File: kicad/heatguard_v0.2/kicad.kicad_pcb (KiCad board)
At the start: 2 copper layers, 100 x 72 mm, 31 parts, among them J11 Conn_01x12, J12 Conn_01x12, J13 Conn_01x12, J14 Conn_01x12, J2 Conn_01x12, J20 Conn_01x01, J3 Conn_01x12, J4 Conn_01x12, J5 Conn_01x12, J6 Conn_01x12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

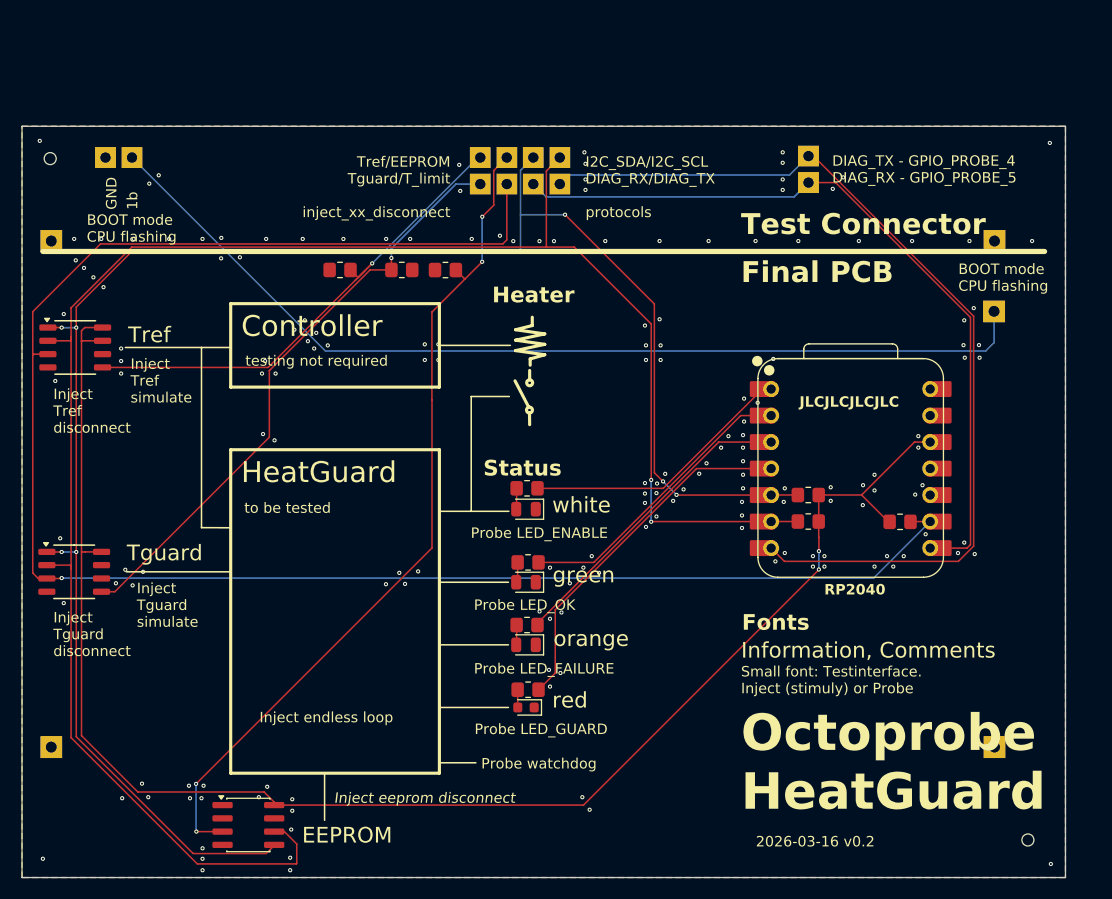
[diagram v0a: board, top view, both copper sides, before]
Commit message: v0.2: XIAO: Now smd (was on pins)
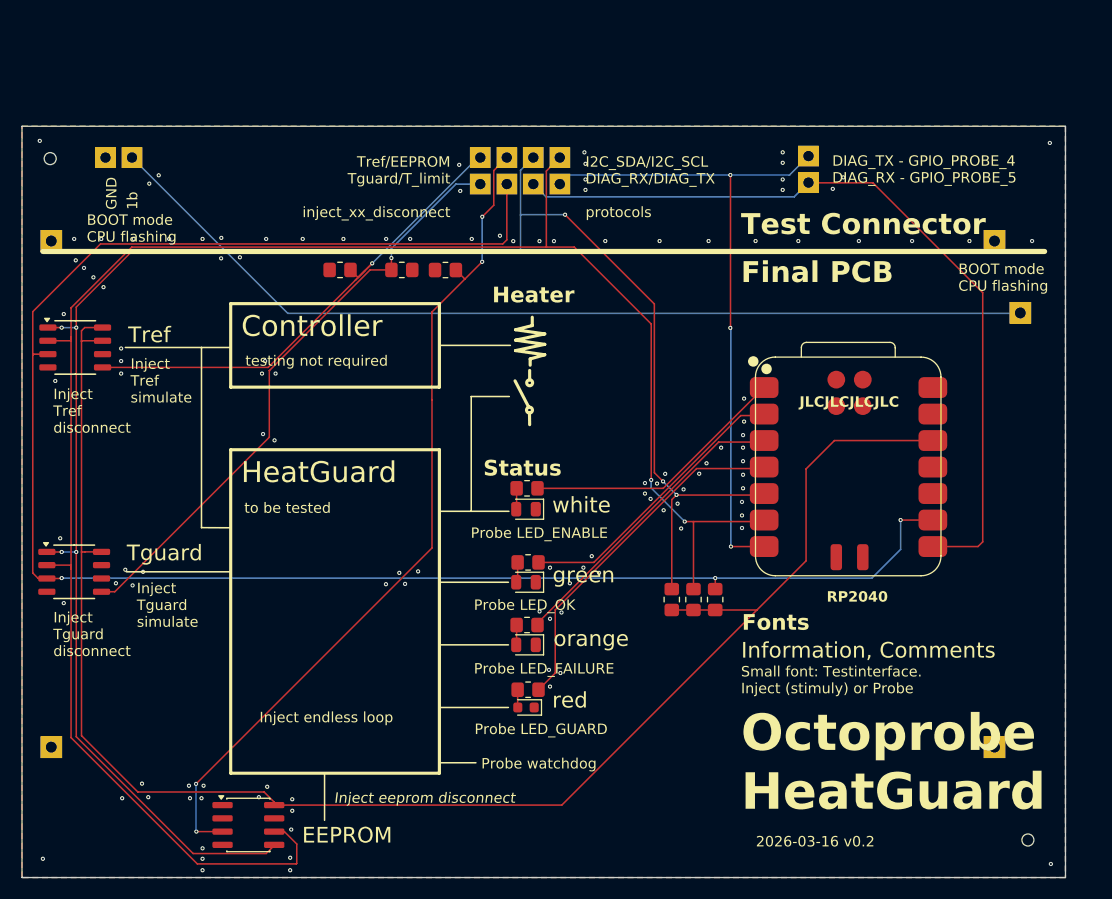
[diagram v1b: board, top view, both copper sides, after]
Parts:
- U4: footprint 00_project_library:XIAO-RP2040-DIP -> 00_project_library:XIAO-RP2040-SMD
- moved R10 19.2 mm to (114.4, 106.4), turned to -90 degrees
- moved R5 16.5 mm to (110.3, 106.4), turned to -90 degrees
- moved U4 13.8 mm to (118.3, 104.2), turned to 0 degrees
- moved R6 13.3 mm to (112.3, 106.4), turned to -90 degrees
- moved J20 2.51 mm to (143.7, 78.9)
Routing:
- net /DIAG_TX: track 88.0 -> 62.5 mm, vias 0 -> 3
- net /I2C_SDA: track 171.4 -> 178.0 mm
- net +3V3: track 151.5 -> 157.2 mm, vias 2 -> 0
- net /DIAG_RX: track 74.1 -> 77.3 mm
- net /BOOT: track 93.6 -> 91.3 mm
- net /I2C_SCL: track 180.0 -> 182.0 mm
- net /inject_T_limit: track 170.5 -> 171.7 mm, vias 1 -> 3
- net GND: vias 172 -> 118

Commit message: v0.2 ready for review
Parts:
- removed J11, J12, J13, J14: Conn_01x12, 00_project_library:octoprobe_breakout_PB_NC
- removed J2, J3, J4, J5, J6: Conn_01x12, 00_project_library:PinSocket_1x2_P2.54mm_Vertical_squarepad
- added D10: LED WHITE, LED_SMD:LED_0805_2012Metric, F.Cu at (50.5, 88.5)
- added D11: LED WHITE, LED_SMD:LED_0805_2012Metric, F.Cu at (49.7, 109.7)
- added D12: LED WHITE, LED_SMD:LED_0805_2012Metric, F.Cu at (78.4, 129.9)
- added J1: Conn_02x02_Odd_Even, 00_project_library:PinHeader_2x02_P2.54mm_Vertical_back, F.Cu at (50.5, 53.1)
- added J8: Conn_02x04_Odd_Even, 00_project_library:PinHeader_2x04_P2.54mm_Vertical_back, F.Cu at (88.9, 55.7)
- added J9: Conn_02x04_Odd_Even, 00_project_library:PinHeader_2x04_P2.54mm_Vertical_back, F.Cu at (106.4, 130.7)
- added R11: 2k2, Resistor_SMD:R_0805_2012Metric_Pad1.20x1.40mm_HandSolder, F.Cu at (50.5, 92.5)
- added R12: 2k2, Resistor_SMD:R_0805_2012Metric_Pad1.20x1.40mm_HandSolder, F.Cu at (49.7, 113.4)
- added R13: 2k2, Resistor_SMD:R_0805_2012Metric_Pad1.20x1.40mm_HandSolder, F.Cu at (82.4, 129.9)
- moved TH1 94.3 mm to (145.0, 64.0)
- moved TH2 93.4 mm to (51.0, 130.0)
- moved J20 22.5 mm to (143.8, 101.4)
- moved J7 2.00 mm to (121.4, 63.9)
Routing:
- net /BOOT: track 91.3 -> 126.8 mm
- net /inject_tref_disconnect: track 48.5 -> 67.0 mm, vias 1 -> 3
- net /inject_tguard_disconnect: track 57.3 -> 75.3 mm, vias 1 -> 3
- net /inject_eeprom_disconnect: track 80.7 -> 97.6 mm
- net /I2C_SCL: track 182.0 -> 193.2 mm
- net /I2C_SDA: track 178.0 -> 188.3 mm
- net /DIAG_TX: track 62.5 -> 71.4 mm
- net /DIAG_RX: track 77.3 -> 85.1 mm, vias 0 -> 1
- net GND: track 0.00 -> 5.99 mm, vias 118 -> 132
- net /LED_OK: track 27.3 -> 25.2 mm
- net Net-(D12-K): track 0.00 -> 1.98 mm
- net Net-(D10-K): track 0.00 -> 1.97 mm
- net Net-(D11-K): track 0.00 -> 1.72 mm
- net /inject_T_limit: track 171.7 -> 170.7 mm
- net /LED_ENABLE: track 25.5 -> 25.2 mm, vias 0 -> 2
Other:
- board size 100 x 72 mm -> 100 x 82 mm
- board text added: "ENABLE white"
- board text added: "FAILURE orange"
- board text added: "GUARD red"
- board text added: "OK green"
- board text added: "inject_xx_disconnect Tref/EEPROM Tguard/T_limit"
- board text added: "protocols I2C_SDA/I2C_SCL DIAG_RX/DIAG_TX"
- board text removed: "I2C_SDA/I2C_SCL DIAG_RX/DIAG_TX protocols"
- board text removed: "Status"
- board text removed: "Tref/EEPROM Tguard/T_limit inject_xx_disconnect"
- board text removed: "green"
- board text removed: "orange"
- board text removed: "red"
- board text removed: "white"

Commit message: Remove all vias
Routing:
- net GND: vias 132 -> 11
- net (no net): vias 1 -> 0

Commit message: v0.2 as ordered
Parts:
- moved R10 54.0 mm to (73.0, 71.7), turned to 180 degrees
- moved R5 34.7 mm to (106.5, 71.8), turned to 180 degrees
- moved R6 32.6 mm to (109.9, 73.9), turned to 180 degrees
- moved R4 30.4 mm to (109.8, 87.7)
- moved R3 27.2 mm to (109.8, 85.1)
- moved R2 24.2 mm to (109.8, 82.6)
- moved R1 20.6 mm to (109.8, 80.0)
- moved J20 6.00 mm to (143.8, 95.4)
- moved U4 6.00 mm to (118.3, 98.2)
- moved D4 3.48 mm to (94.8, 94.5), turned to 90 degrees
- moved D1 3.42 mm to (94.8, 101.6), turned to 90 degrees
- moved R9 3.36 mm to (89.9, 71.7)
- moved R7 3.14 mm to (79.2, 71.7)
- moved R8 3.08 mm to (84.4, 71.7)
- moved J7 2.54 mm to (121.4, 66.4), turned to 180 degrees
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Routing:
- net Net-(D3-A): track 1.69 -> 36.1 mm
- net Net-(D2-A): track 1.86 -> 30.0 mm
- net /LED_GUARD: track 33.8 -> 7.75 mm
- net Net-(D1-A): track 1.76 -> 23.9 mm
- net /LED_FAILURE: track 28.8 -> 7.77 mm
- net +3V3: track 157.2 -> 175.7 mm, vias 0 -> 2
- net /LED_ENABLE: track 25.2 -> 7.77 mm, vias 2 -> 0
- net /LED_OK: track 25.2 -> 7.76 mm
- net Net-(D4-A): track 1.96 -> 19.2 mm
- net /DIAG_TX: track 71.4 -> 63.8 mm, vias 3 -> 0
- net /I2C_SDA: track 188.3 -> 181.6 mm, vias 8 -> 5
- net /DIAG_RX: track 85.1 -> 79.5 mm, vias 1 -> 2
- net /I2C_SCL: track 193.2 -> 187.7 mm
- net /inject_T_limit: track 170.7 -> 167.0 mm, vias 3 -> 4
- net /BOOT: track 126.8 -> 124.4 mm
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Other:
- board text added: "DIAG_RX - GPIO_PROBE_5 DIAG_TX - GPIO_PROBE_4"
- board text added: "Fonts:"
- board text removed: "Controller"
- board text removed: "DIAG_TX - GPIO_PROBE_4 DIAG_RX - GPIO_PROBE_5"
- board text removed: "Fonts"
- board text removed: "testing not required"
